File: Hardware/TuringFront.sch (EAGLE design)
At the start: 64 parts, among them T1 2N3904, U1 TL074_

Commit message: Starting to route front board
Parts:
- removed FRONT_BUS: (no value), MusicThingModular:MA07-2_BACKSIDEBACKSIDE
- added SV1: (no value), MusicThingModular:10PIN_BACKSIDE
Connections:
- net +12V_FRONT: now also C7.2, R20.1, R23.2, R29.1, R3.1; no longer C7.1, R20.2, R23.1, R29.2, R3.2
- net -12V_FRONT: now also C14.2, C8.1, C9.2, R35.2; no longer C14.1, C8.2, C9.1, R35.1
- net B1_FRONT: now also SV1.1; no longer FRONT_BUS.1
- net B2_FRONT: now also SV1.2; no longer FRONT_BUS.2
- net B3_FRONT: now also SV1.3; no longer FRONT_BUS.3
- net B4_FRONT: now also SV1.4; no longer FRONT_BUS.4
- net B5_FRONT: now also SV1.5; no longer FRONT_BUS.5
- net B6_FRONT: now also SV1.6; no longer FRONT_BUS.6
- net B7_FRONT: now also SV1.7; no longer FRONT_BUS.7
- net B8_FRONT: now also SV1.8; no longer FRONT_BUS.8
- net CLOCK_FRONT: now also R13.1, SV1.9; no longer FRONT_BUS.9, R13.2
- net GND_FRONT: now also C14.1, C16.1, C7.1, C8.2, R11.1, R9.1, U1D.+IN; no longer C14.2, C16.2, C7.2, C8.1, R11.2, R9.2, U1B.+IN
- net LOOP_CTRL_FRONT: now also R22.2; no longer R22.1
- net MAIN_OUT: now also U1A.OUT; no longer U1C.OUT
- net N$12: now also C16.2, R3.2, R9.2, U1B.-IN; no longer C16.1, R3.1, R9.1, U1D.-IN
- net N$13: now also U1A.-IN; no longer U1C.-IN
- net N$15: now also R13.2; no longer R13.1
- net N$16: now also C10.2, R29.2; no longer C10.1, R29.1
- net N$18: now also R20.2, R28.2; no longer R20.1, R28.1
- net N$20: now also C10.1; no longer C10.2
- net N$21: now also U1C.-IN; no longer U1A.-IN
- net N$22: now also U1C.OUT; no longer U1A.OUT
- net N$25: now also C9.1; no longer C9.2
- net N$26: now also R28.1; no longer R28.2
- net N$27: now also R32.1, U1D.-IN; no longer R32.2, U1B.-IN
- net N$41: now also U1D.OUT; no longer U1B.OUT
- net N$43: now also R22.1; no longer R22.2
- net N$47: now also R23.1; no longer R23.2
- net N$48: now also R35.1; no longer R35.2
- net N$5: now also U1B.+IN; no longer U1D.+IN
- net N$6: now also R17.2; no longer R17.1
- net N$8: now also U1B.OUT; no longer U1D.OUT
- net N$9: now also R32.2; no longer R32.1
- net NOISE_FRONT: now also R11.2; no longer R11.1
- net PULSE_OUT_FRONT: now also R17.1, SV1.10; no longer FRONT_BUS.10, R17.2
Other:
- note removed: "Optional reverse polarity protection If not required, omit diodes and replace fuses with jumper wire. Don't get it the wrong way around! Ferrites: 81-BL01RN1A1D2B or 623-2743001112LF"

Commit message: Layouts
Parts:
- removed RN2: 2.2k, resistor-net:RN08
- added R1, R14, R15, R16, R21, R4, R6, R8: 2.2k, TomW:R-EU_0207/7
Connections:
- net CLOCK_FRONT: now also R12.1, R7.1; no longer R12.2, R7.2
- net GND_FRONT: now also R1.2, R12.2, R14.1, R15.1, R16.1, R21.1, R4.2, R6.2, R8.2; no longer R12.1, RN2.1
- net N$30: now also R1.1; no longer RN2.9
- net N$31: now also R4.1; no longer RN2.8
- net N$32: now also R6.1; no longer RN2.7
- net N$33: now also R8.1; no longer RN2.6
- net N$34: now also R14.2; no longer RN2.5
- net N$35: now also R15.2; no longer RN2.4
- net N$36: now also R16.2; no longer RN2.3
- net N$37: now also R21.2; no longer RN2.2
- net N$5: now also R7.2; no longer R7.1
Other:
- moved on the sheet: R13, R22, R23, R35, R9

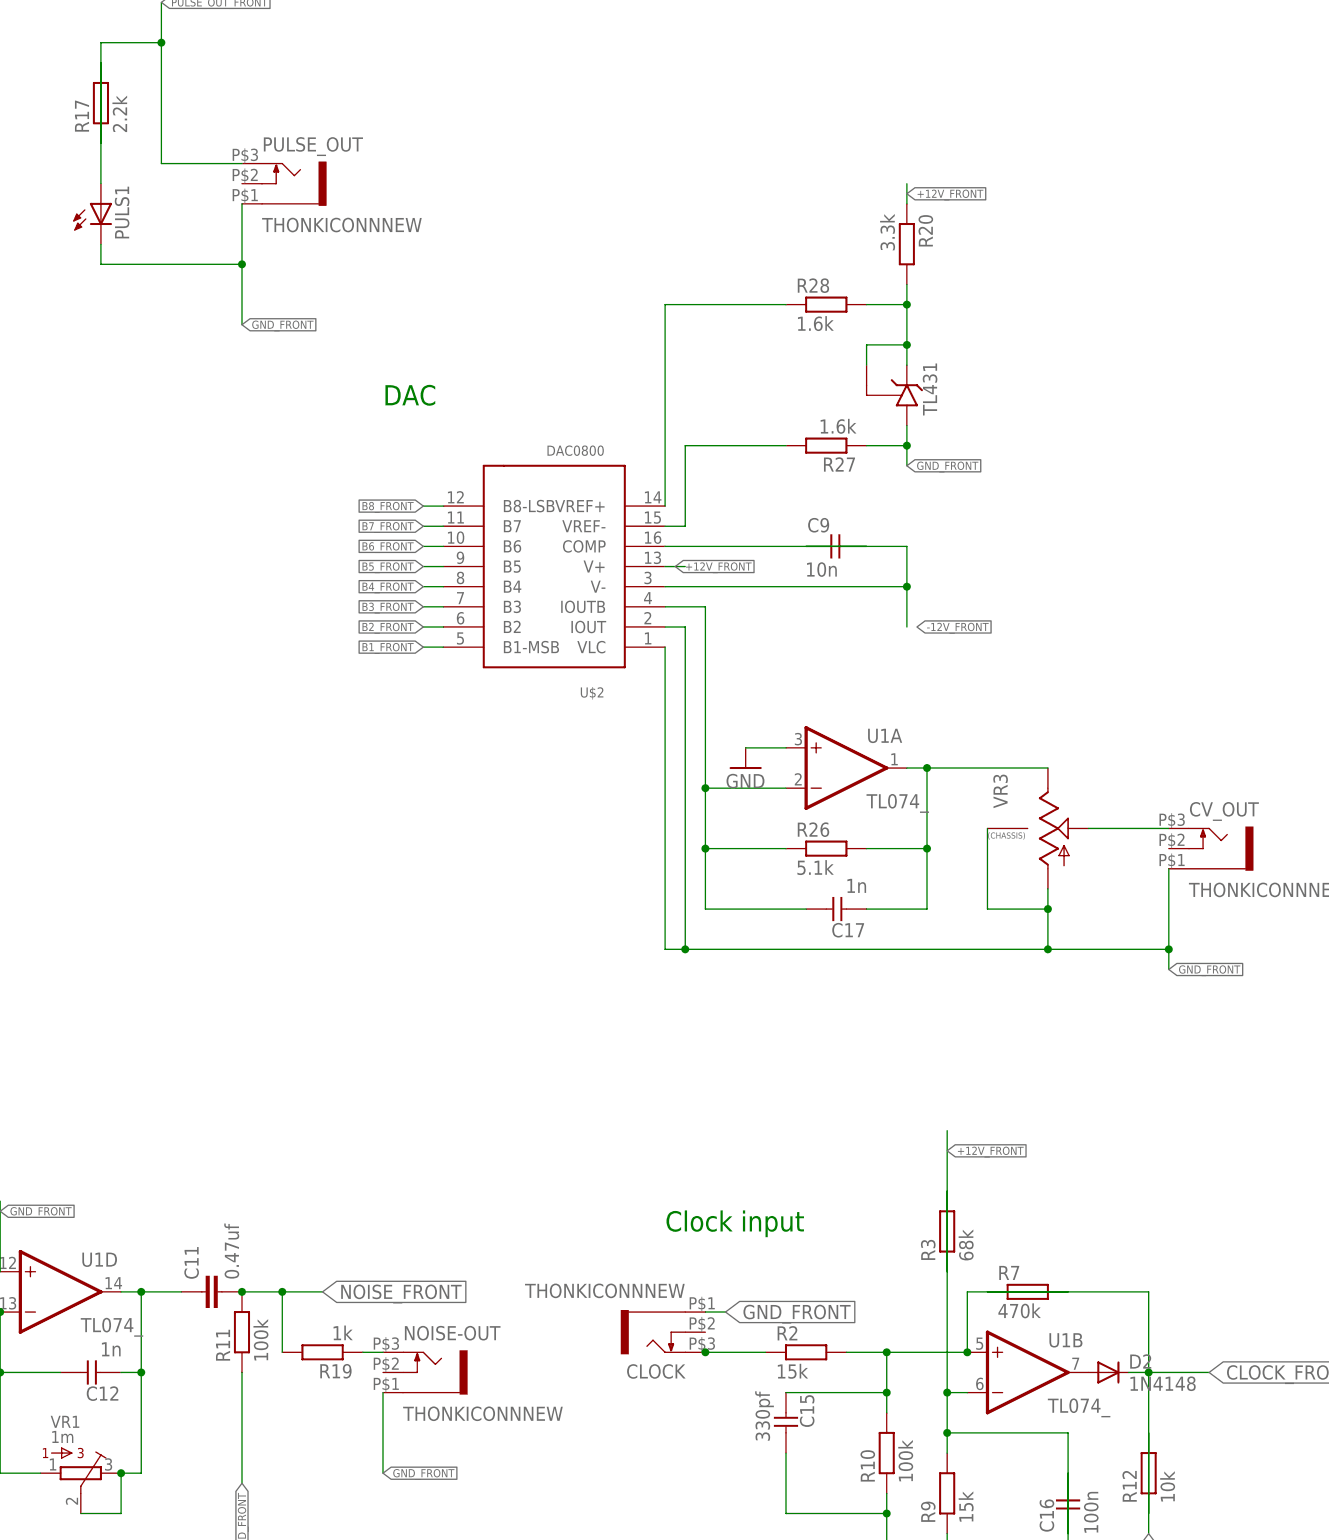
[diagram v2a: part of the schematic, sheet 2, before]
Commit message: routing tweaks on back panel
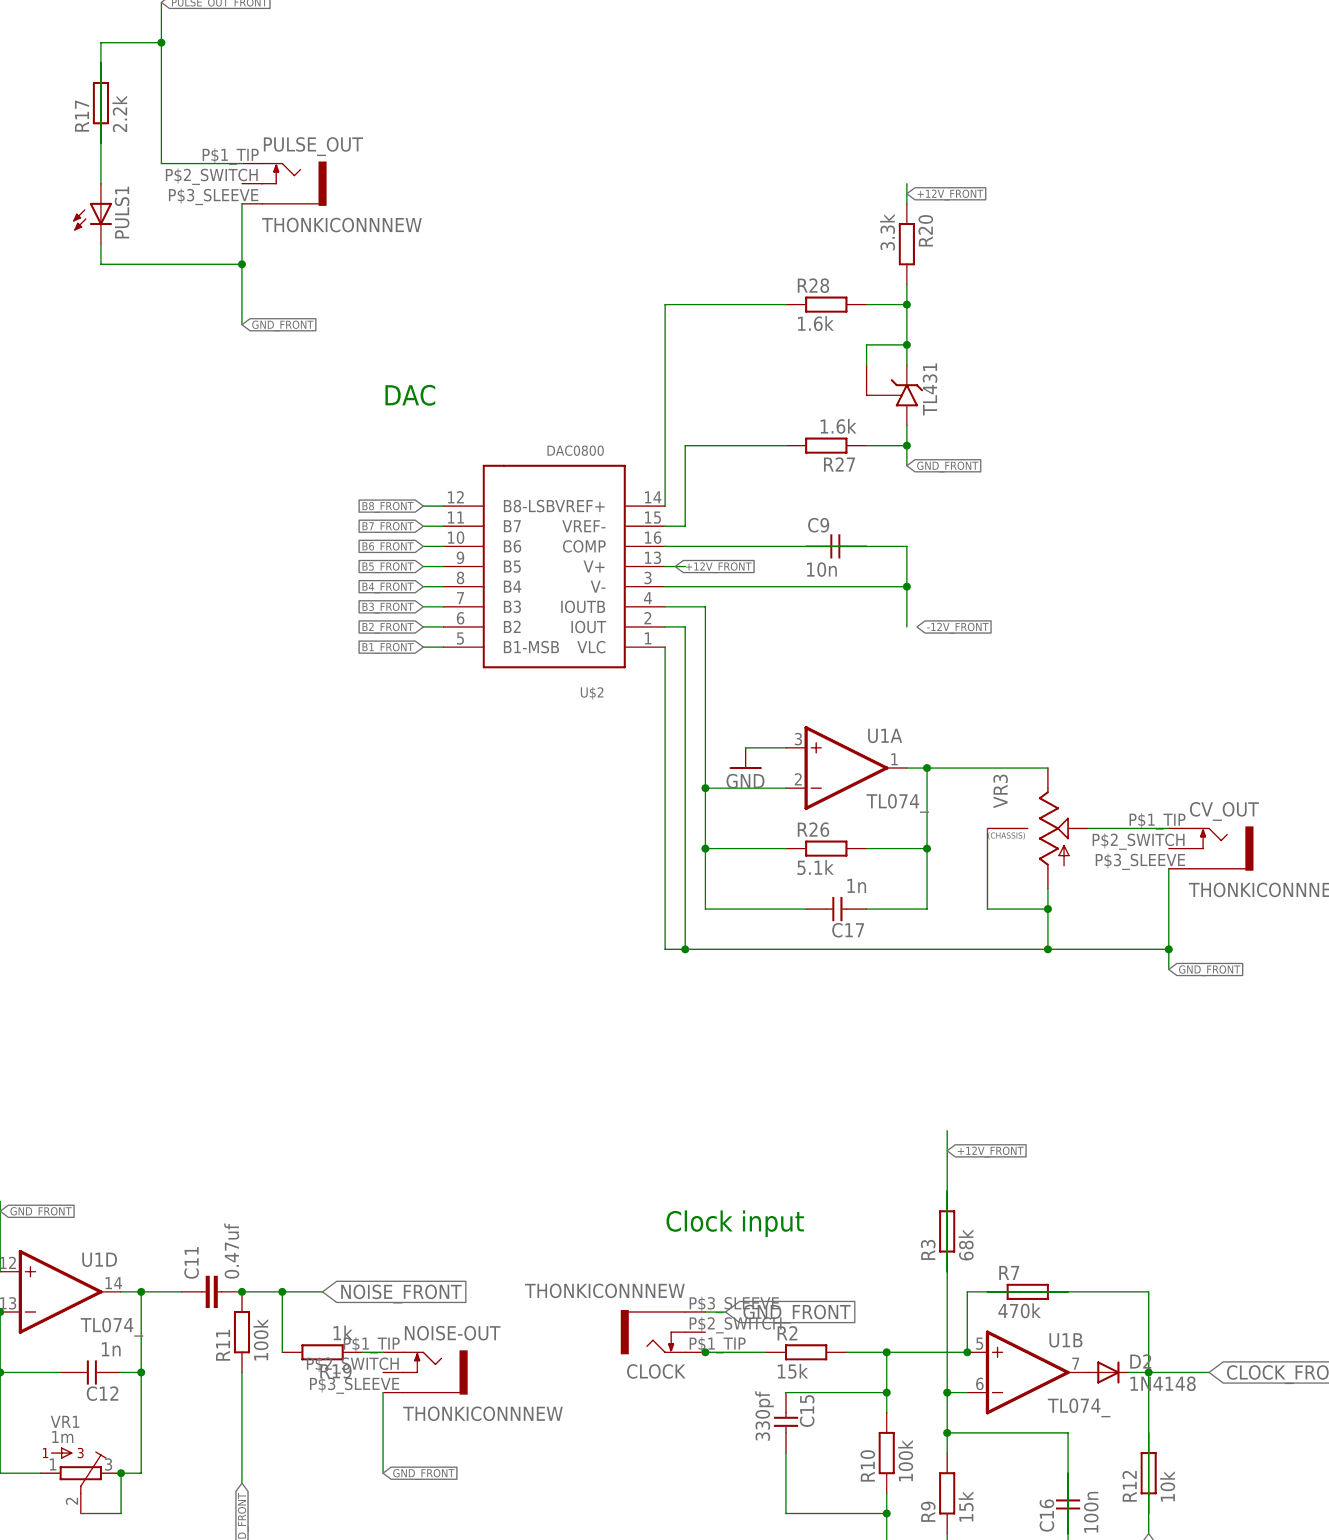
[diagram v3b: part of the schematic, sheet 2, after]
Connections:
- net GND_FRONT: now also CLOCK.SLEEVE, CV_IN.SLEEVE, CV_OUT.SLEEVE, NOISE-OUT.SLEEVE, PULSE_OUT.SLEEVE; no longer CLOCK.5, CV_IN.5, CV_OUT.5, NOISE-OUT.5, PULSE_OUT.5
- net N$2: now also CLOCK.TIP; no longer CLOCK.3
- net N$3: now also CV_IN.TIP; no longer CV_IN.3
- net N$39: now also CV_OUT.TIP; no longer CV_OUT.3
- net N$40: now also NOISE-OUT.TIP; no longer NOISE-OUT.3
- net PULSE_OUT_FRONT: now also PULSE_OUT.TIP; no longer PULSE_OUT.3
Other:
- moved on the sheet: CLOCK, CV_IN, CV_OUT, NOISE-OUT, PULSE_OUT
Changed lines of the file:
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@@
 <?xml version="1.0" encoding="utf-8"?>
 <!DOCTYPE eagle SYSTEM "eagle.dtd">
-<eagle version="6.6.0">
+<eagle version="7.4.0">
 <drawing>
 <settings>
@@
 <net name="N$3" class="0">
 <segment>
-<pinref part="CV_IN" gate="G$1" pin="3"/>
+<pinref part="CV_IN" gate="G$1" pin="TIP"/>
 <wire x1="83.82" y1="203.2" x2="76.2" y2="203.2" width="0.1524" layer="91"/>
 <pinref part="R5" gate="G$1" pin="1"/>
@@
 </segment>
 <segment>
-<pinref part="CV_IN" gate="G$1" pin="5"/>
+<pinref part="CV_IN" gate="G$1" pin="SLEEVE"/>
 <wire x1="81.28" y1="208.28" x2="76.2" y2="208.28" width="0.1524" layer="91"/>
 <label x="81.28" y="208.28" size="1.016" layer="95" xref="yes"/>
@@
 <net name="N$2" class="0">
 <segment>
-<pinref part="CLOCK" gate="G$1" pin="3"/>
-<pinref part="CLOCK" gate="G$1" pin="3"/>
+<pinref part="CLOCK" gate="G$1" pin="TIP"/>
+<pinref part="CLOCK" gate="G$1" pin="TIP"/>
 <pinref part="R2" gate="G$1" pin="1"/>
 <wire x1="299.72" y1="76.2" x2="307.34" y2="76.2" width="0.1524" layer="91"/>
@@
 <net name="N$39" class="0">
 <segment>
-<pinref part="CV_OUT" gate="G$1" pin="3"/>
+<pinref part="CV_OUT" gate="G$1" pin="TIP"/>
 <wire x1="347.98" y1="142.24" x2="358.14" y2="142.24" width="0.1524" layer="91"/>
 <pinref part="VR3" gate="G$1" pin="S"/>
@@
 <net name="N$40" class="0">
 <segment>
-<pinref part="NOISE-OUT" gate="G$1" pin="3"/>
+<pinref part="NOISE-OUT" gate="G$1" pin="TIP"/>
 <pinref part="R19" gate="G$1" pin="1"/>
 <wire x1="259.08" y1="76.2" x2="256.54" y2="76.2" width="0.1524" layer="91"/>
@@
 </segment>
 <segment>
-<pinref part="NOISE-OUT" gate="G$1" pin="5"/>
+<pinref part="NOISE-OUT" gate="G$1" pin="SLEEVE"/>
 <wire x1="259.08" y1="71.12" x2="259.08" y2="60.96" width="0.1524" layer="91"/>
 <label x="259.08" y="60.96" size="1.016" layer="95" xref="yes"/>
@@
 </segment>
 <segment>
-<pinref part="CLOCK" gate="G$1" pin="5"/>
+<pinref part="CLOCK" gate="G$1" pin="SLEEVE"/>
 <wire x1="302.26" y1="81.28" x2="299.72" y2="81.28" width="0.1524" layer="91"/>
 <label x="302.26" y="81.28" size="1.778" layer="95" xref="yes"/>
@@
 <wire x1="335.28" y1="132.08" x2="342.9" y2="132.08" width="0.1524" layer="91"/>
 <junction x="342.9" y="132.08"/>
-<pinref part="CV_OUT" gate="G$1" pin="5"/>
+<pinref part="CV_OUT" gate="G$1" pin="SLEEVE"/>
 <wire x1="358.14" y1="137.16" x2="358.14" y2="127" width="0.1524" layer="91"/>
 <wire x1="342.9" y1="127" x2="358.14" y2="127" width="0.1524" layer="91"/>
@@
 </segment>
 <segment>
-<pinref part="PULSE_OUT" gate="G$1" pin="5"/>
+<pinref part="PULSE_OUT" gate="G$1" pin="SLEEVE"/>
 <wire x1="241.3" y1="220.98" x2="241.3" y2="213.36" width="0.1524" layer="91"/>
 <label x="241.3" y="205.74" size="1.016" layer="95" xref="yes"/>
@@
 <net name="PULSE_OUT_FRONT" class="0">
 <segment>
-<pinref part="PULSE_OUT" gate="G$1" pin="3"/>
+<pinref part="PULSE_OUT" gate="G$1" pin="TIP"/>
 <wire x1="241.3" y1="226.06" x2="231.14" y2="226.06" width="0.1524" layer="91"/>
 <wire x1="231.14" y1="226.06" x2="231.14" y2="241.3" width="0.1524" layer="91"/>

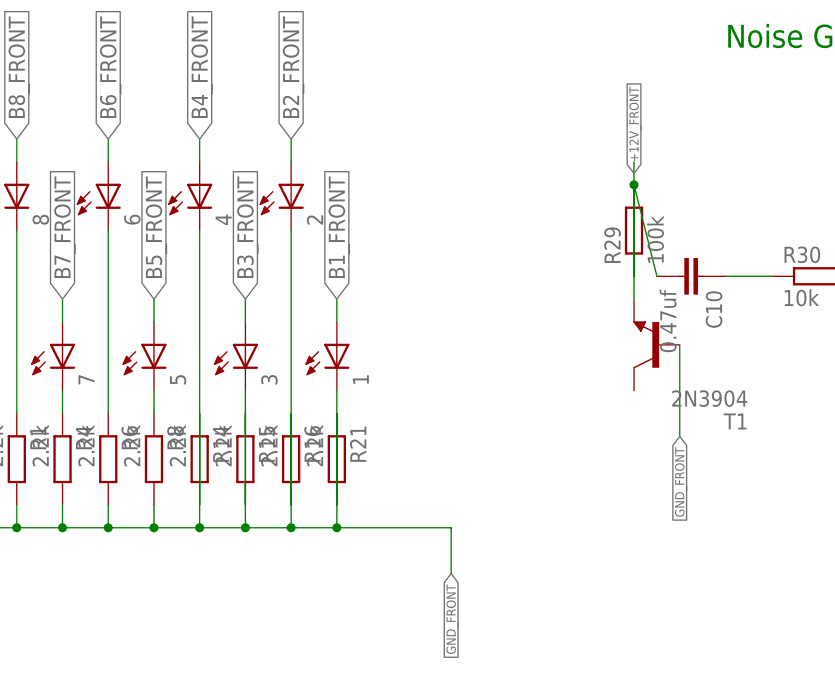
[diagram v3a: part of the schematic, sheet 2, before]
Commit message: Front board routed awaiting checking and optimisation
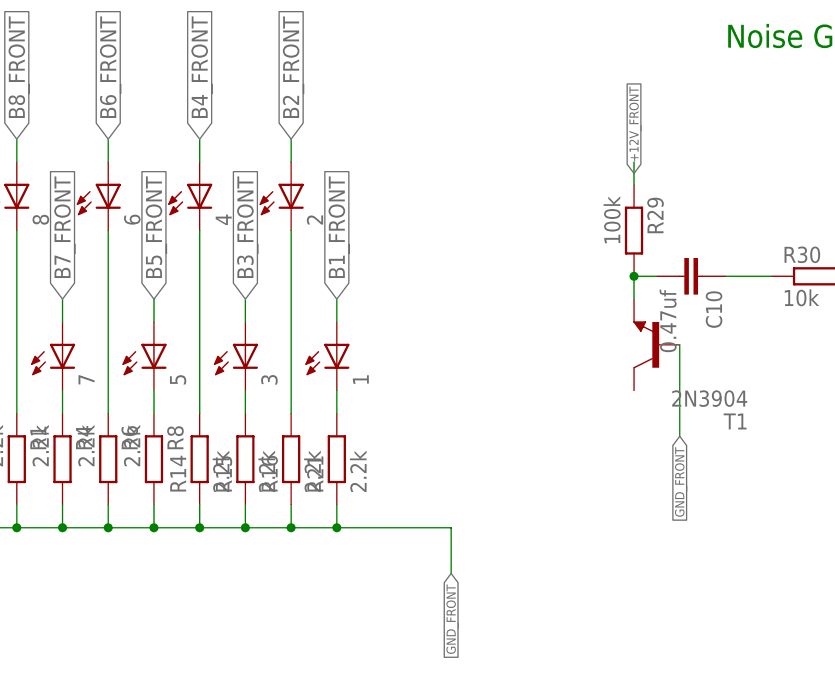
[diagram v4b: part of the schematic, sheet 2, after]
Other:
- moved on the sheet: R14, R15, R16, R21, R29
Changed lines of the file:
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@@
 </segment>
 </net>
-<net name="LOOP_CTRL_FRONT" class="1">
+<net name="LOOP_CTRL_FRONT" class="0">
 <segment>
 <pinref part="R5" gate="G$1" pin="2"/>
@@
 <instance part="C13" gate="G$1" x="88.9" y="200.66"/>
 <instance part="T1" gate="G1" x="144.78" y="71.12" rot="R180"/>
-<instance part="R29" gate="G$1" x="142.24" y="83.82" rot="R90"/>
+<instance part="R29" gate="G$1" x="142.24" y="83.82" rot="R270"/>
 <instance part="C10" gate="G$1" x="149.86" y="78.74" rot="R270"/>
 <instance part="R30" gate="G$1" x="162.56" y="78.74"/>
@@
 <instance part="R6" gate="G$1" x="83.82" y="58.42" rot="R270"/>
 <instance part="R8" gate="G$1" x="88.9" y="58.42" rot="R270"/>
-<instance part="R14" gate="G$1" x="93.98" y="58.42" rot="R270"/>
-<instance part="R15" gate="G$1" x="99.06" y="58.42" rot="R270"/>
-<instance part="R16" gate="G$1" x="104.14" y="58.42" rot="R270"/>
-<instance part="R21" gate="G$1" x="109.22" y="58.42" rot="R270"/>
+<instance part="R14" gate="G$1" x="93.98" y="58.42" rot="R90"/>
+<instance part="R15" gate="G$1" x="99.06" y="58.42" rot="R90"/>
+<instance part="R16" gate="G$1" x="104.14" y="58.42" rot="R90"/>
+<instance part="R21" gate="G$1" x="109.22" y="58.42" rot="R90"/>
 </instances>
 <busses>
@@
 <segment>
 <pinref part="R29" gate="G$1" pin="1"/>
-<wire x1="142.24" y1="91.44" x2="142.24" y2="78.74" width="0.1524" layer="91"/>
+<wire x1="142.24" y1="91.44" x2="142.24" y2="88.9" width="0.1524" layer="91"/>
 <label x="142.24" y="90.17" size="1.016" layer="95" rot="R90" xref="yes"/>
 </segment>
@@
 <net name="N$34" class="0">
 <segment>
-<wire x1="93.98" y1="83.82" x2="93.98" y2="53.34" width="0.1524" layer="91"/>
+<wire x1="93.98" y1="83.82" x2="93.98" y2="63.5" width="0.1524" layer="91"/>
 <pinref part="4" gate="G$1" pin="C"/>
 <pinref part="R14" gate="G$1" pin="2"/>
@@
 <net name="N$35" class="0">
 <segment>
-<wire x1="99.06" y1="66.04" x2="99.06" y2="53.34" width="0.1524" layer="91"/>
+<wire x1="99.06" y1="66.04" x2="99.06" y2="63.5" width="0.1524" layer="91"/>
 <pinref part="3" gate="G$1" pin="C"/>
 <pinref part="R15" gate="G$1" pin="2"/>
@@
 <net name="N$36" class="0">
 <segment>
-<wire x1="104.14" y1="83.82" x2="104.14" y2="53.34" width="0.1524" layer="91"/>
+<wire x1="104.14" y1="83.82" x2="104.14" y2="63.5" width="0.1524" layer="91"/>
 <pinref part="2" gate="G$1" pin="C"/>
 <pinref part="R16" gate="G$1" pin="2"/>
@@
 <net name="N$37" class="0">
 <segment>
-<wire x1="109.22" y1="66.04" x2="109.22" y2="53.34" width="0.1524" layer="91"/>
+<wire x1="109.22" y1="66.04" x2="109.22" y2="63.5" width="0.1524" layer="91"/>
 <pinref part="1" gate="G$1" pin="C"/>
 <pinref part="R21" gate="G$1" pin="2"/>
@@
 <pinref part="T1" gate="G1" pin="E"/>
 <pinref part="R29" gate="G$1" pin="2"/>
-<wire x1="142.24" y1="76.2" x2="142.24" y2="88.9" width="0.1524" layer="91"/>
+<wire x1="142.24" y1="76.2" x2="142.24" y2="78.74" width="0.1524" layer="91"/>
 <pinref part="C10" gate="G$1" pin="2"/>
-<wire x1="144.78" y1="78.74" x2="142.24" y2="88.9" width="0.1524" layer="91"/>
-<junction x="142.24" y="88.9"/>
+<wire x1="144.78" y1="78.74" x2="142.24" y2="78.74" width="0.1524" layer="91"/>
+<junction x="142.24" y="78.74"/>
 </segment>
 </net>
@@
 <junction x="88.9" y="50.8"/>
 <pinref part="R14" gate="G$1" pin="1"/>
-<wire x1="93.98" y1="63.5" x2="93.98" y2="50.8" width="0.1524" layer="91"/>
+<wire x1="93.98" y1="53.34" x2="93.98" y2="50.8" width="0.1524" layer="91"/>
 <junction x="93.98" y="50.8"/>
 <pinref part="R15" gate="G$1" pin="1"/>
-<wire x1="99.06" y1="63.5" x2="99.06" y2="50.8" width="0.1524" layer="91"/>
+<wire x1="99.06" y1="53.34" x2="99.06" y2="50.8" width="0.1524" layer="91"/>
 <junction x="99.06" y="50.8"/>
 <pinref part="R16" gate="G$1" pin="1"/>
-<wire x1="104.14" y1="63.5" x2="104.14" y2="50.8" width="0.1524" layer="91"/>
+<wire x1="104.14" y1="53.34" x2="104.14" y2="50.8" width="0.1524" layer="91"/>
 <junction x="104.14" y="50.8"/>
 <pinref part="R21" gate="G$1" pin="1"/>
-<wire x1="109.22" y1="63.5" x2="109.22" y2="50.8" width="0.1524" layer="91"/>
+<wire x1="109.22" y1="53.34" x2="109.22" y2="50.8" width="0.1524" layer="91"/>
 <junction x="109.22" y="50.8"/>
 </segment>

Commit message: tidy up schematics
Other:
- note removed: "LED display"
- note removed: "Power and expansion"
